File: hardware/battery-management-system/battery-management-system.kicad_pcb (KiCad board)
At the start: 4 copper layers, 100 x 100 mm, 195 parts, among them IC1 LT8584EFE#PBF, IC2 LT8584EFE#PBF, IC3 LT8584EFE#PBF, IC4 LT8584EFE#PBF, J1 VBAT_DISCHARGE, J10 TEMP_CELL4, J2 CELLS, J3 Charge, J4 Discharge, J5 AMPHENOL_micro_usb_10118194-0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, J6 ARM-JTAG-SWD, J7 TEMP_CELL1, J8 TEMP_CELL2, J9 TEMP_CELL3, Q1 TJ40S04M3L, Q10 BS250FTA, Q11 BS250FTA, Q12 BS250FTA, Q13 BS250FTA, Q14 DMN3404L, Q2 TJ40S04M3L, Q3 DMN3404L, Q4 DMN3404L, Q5 DMN3404L, Q6 DMN3404L, Q7 DMN3404L, Q8 BS250FTA, Q9 DMN3404L, T1 NA6252-ALD, T2 NA6252-ALD, T3 NA6252-ALD, T4 NA6252-ALD, U1 STC3100, U10 LM2904M8-13, U11 LM2904M8-13, U2 L6982CDR, U3 L6982CDR, U4 ICL7660, U5 ICL7660, U6 FT230XS, U7 STM32L071CZTx, U8 AT24C512C, U9 NCT75DR2G

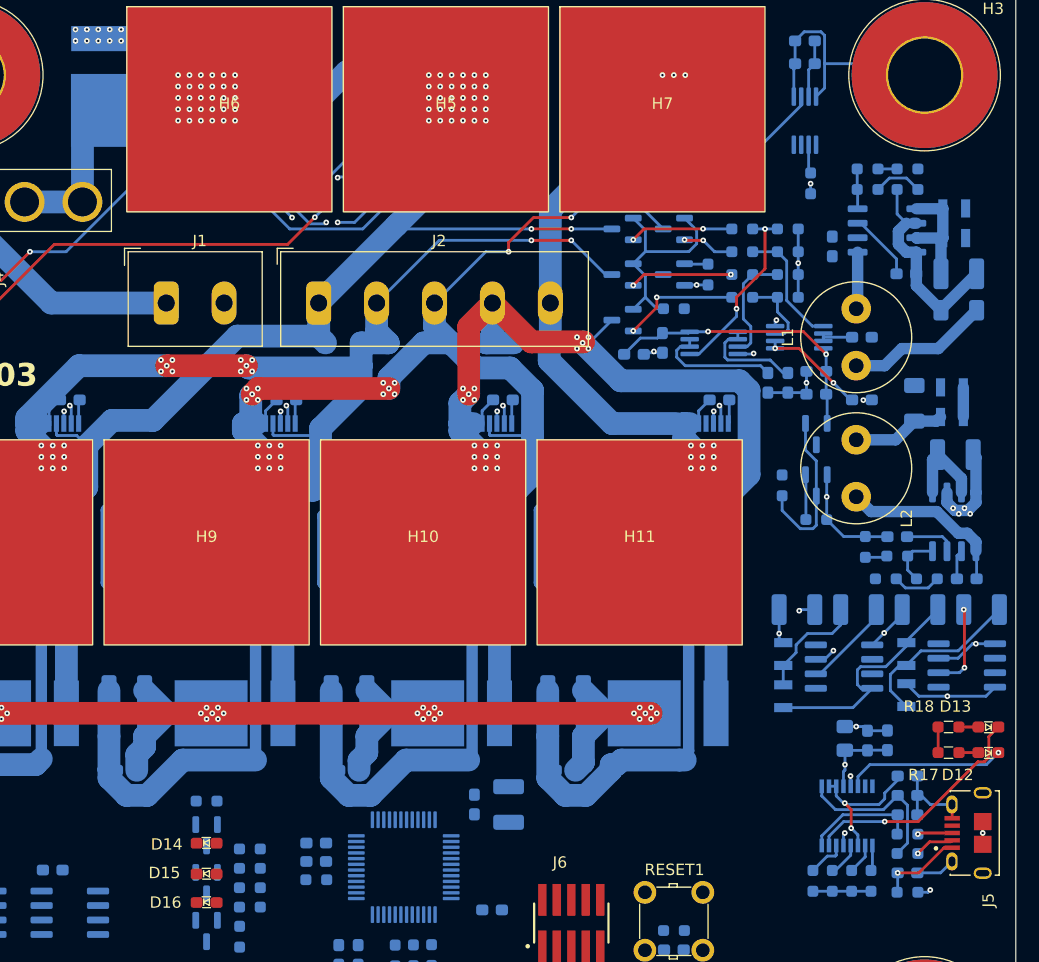
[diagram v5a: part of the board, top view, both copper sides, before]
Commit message: continue work on layout of BMS
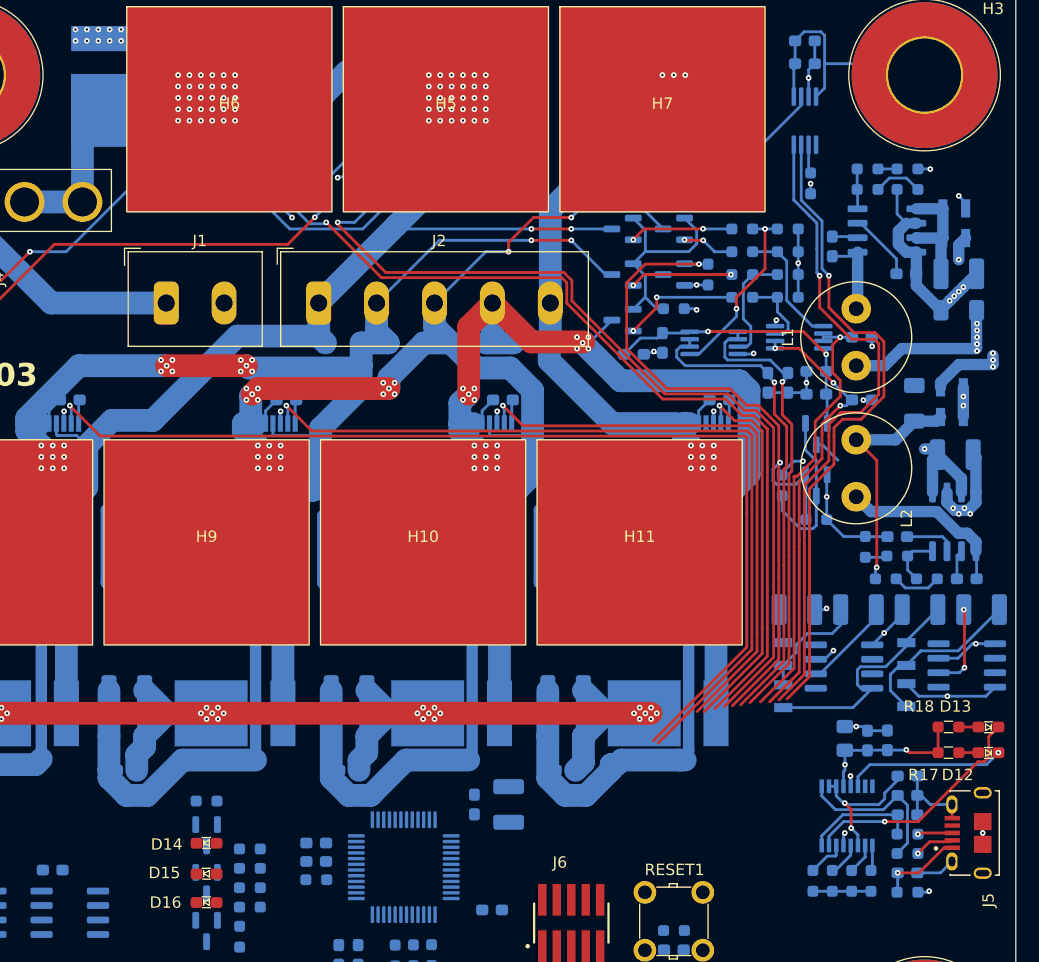
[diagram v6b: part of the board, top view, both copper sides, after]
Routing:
- net /PACK_EXT: track 34.0 -> 128.1 mm, vias 30 -> 32
- net /Cell Balancing/CELL4_ENABLE: track 1.63 -> 92.2 mm
- net /5V_USB: track 10.4 -> 89.9 mm, vias 2 -> 7
- net /DISCHARGE: track 6.10 -> 79.8 mm
- net /CHARGE: track 6.29 -> 79.4 mm
- net /Cell Balancing/CELL3_ENABLE: track 1.63 -> 74.0 mm
- net /EN_CELL_MEASUREMENT: track 6.03 -> 66.4 mm, vias 0 -> 2
- net /MCU/SCL: track 0.00 -> 57.6 mm, vias 0 -> 1
- net /MCU/SDA: track 0.00 -> 57.2 mm, vias 0 -> 1
- net /Cell Balancing/CELL2_ENABLE: track 1.63 -> 51.5 mm
- net /5V: track 11.2 -> 55.8 mm, vias 1 -> 4
- net /Cell Measurement/CELL2: track 3.18 -> 38.9 mm, vias 0 -> 1
- net /Cell Measurement/CELL4: track 11.1 -> 42.6 mm, vias 0 -> 1
- net /Cell Balancing/CELL1_ENABLE: track 1.63 -> 33.0 mm
- net /Cell Measurement/CELL3: track 9.27 -> 40.3 mm, vias 0 -> 1
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
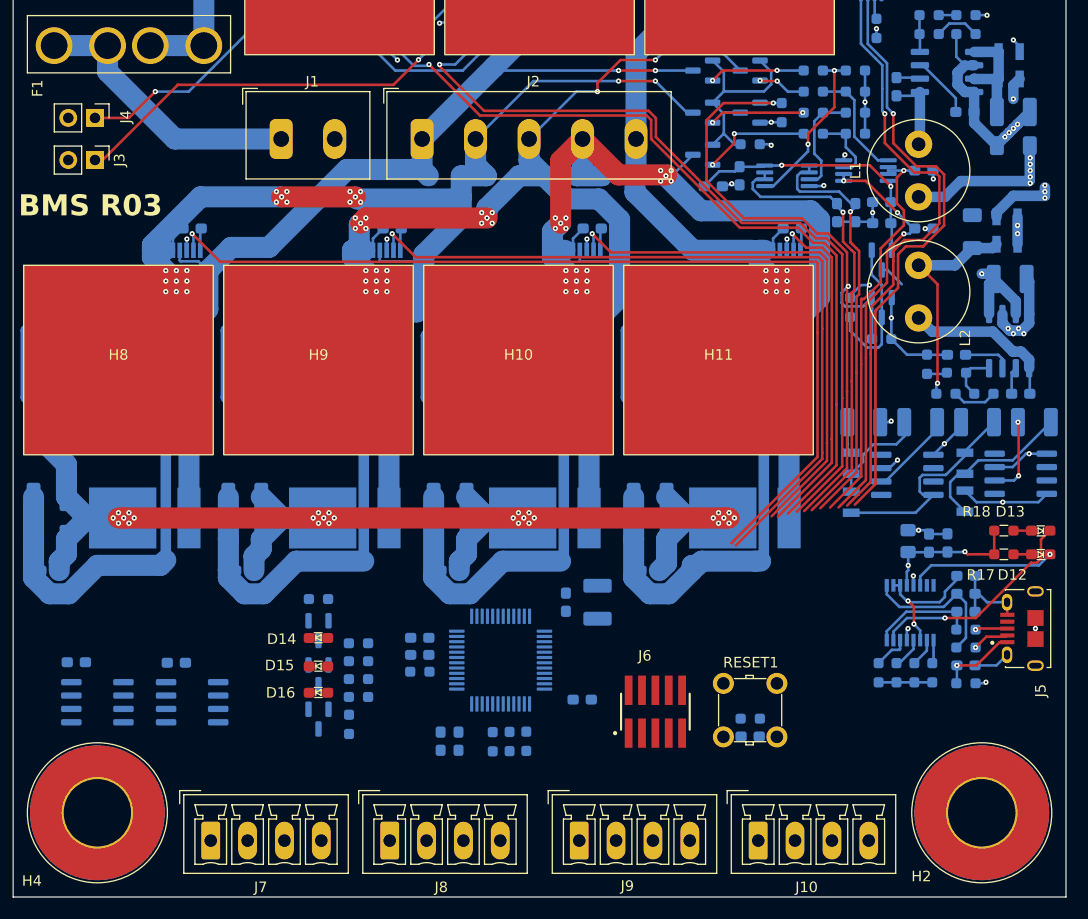
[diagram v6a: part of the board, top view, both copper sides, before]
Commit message: finish layout of BMS
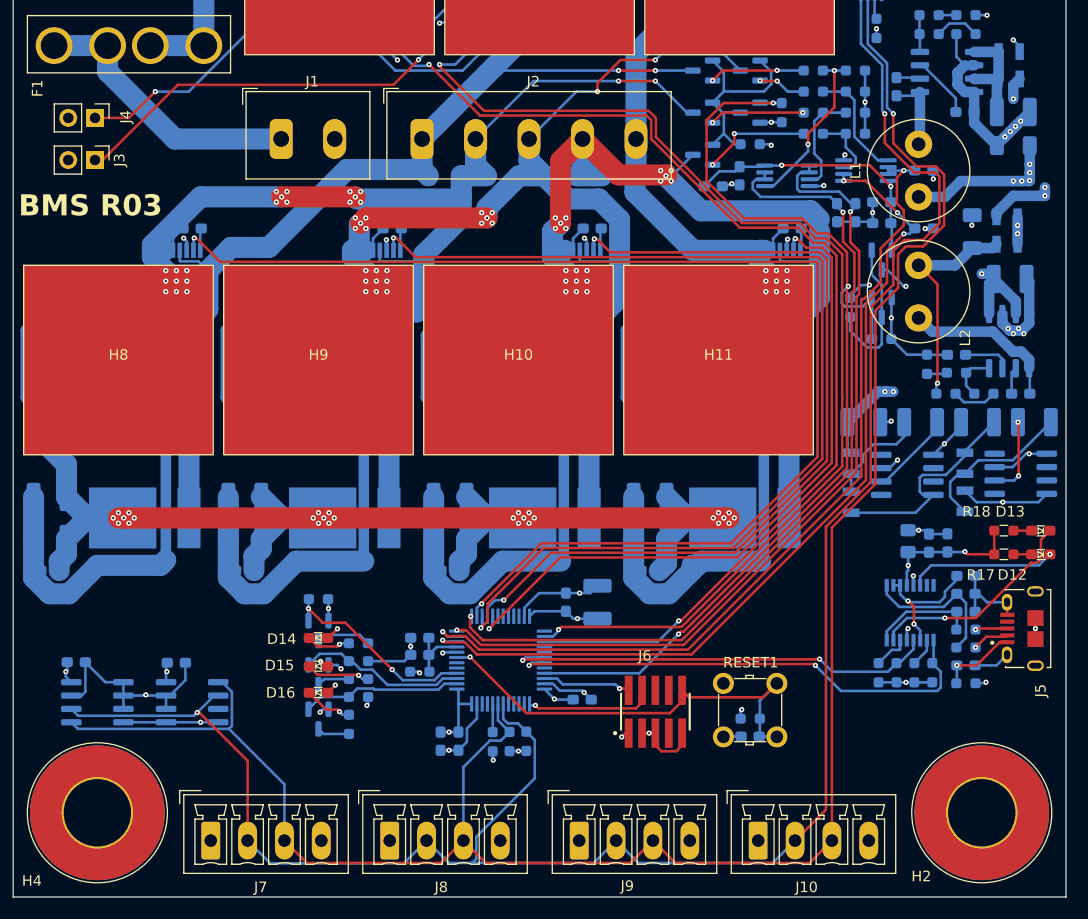
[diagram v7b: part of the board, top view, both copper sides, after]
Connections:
- U7 pad 14: /Cell Balancing/CELL1_ENABLE -> /Cell Balancing/CELL4_ENABLE
- U7 pad 15: /Cell Balancing/CELL2_ENABLE -> /Cell Balancing/CELL3_ENABLE
- U7 pad 16: /Cell Balancing/CELL3_ENABLE -> /Cell Balancing/CELL2_ENABLE
- U7 pad 17: /Cell Balancing/CELL4_ENABLE -> /Cell Balancing/CELL1_ENABLE
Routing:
- net /MCU/SCL: track 57.6 -> 197.8 mm, vias 1 -> 2
- net /MCU/SDA: track 57.2 -> 196.5 mm
- net GND: track 117.1 -> 190.1 mm, vias 45 -> 59
- net /Cell Measurement/CELL1: track 39.1 -> 84.4 mm, vias 3 -> 4
- net /MCU/UART_USB_RX: track 2.24 -> 46.8 mm, vias 0 -> 2
- net /Cell Measurement/CELL2: track 38.9 -> 83.4 mm, vias 1 -> 2
- net /MCU/NRST: track 0.00 -> 42.4 mm, vias 0 -> 1
- net /Cell Measurement/CELL3: track 40.3 -> 80.8 mm, vias 1 -> 2
- net /Cell Measurement/CELL4: track 42.6 -> 81.7 mm, vias 1 -> 2
- net /MCU/UART_USB_TX: track 3.02 -> 41.6 mm, vias 0 -> 2
- net /Cell Balancing/CELL1_ENABLE: track 33.0 -> 65.3 mm, vias 1 -> 2
- net /EN_CELL_MEASUREMENT: track 66.4 -> 97.5 mm, vias 2 -> 3
- net /Cell Balancing/CELL2_ENABLE: track 51.5 -> 82.0 mm, vias 1 -> 2
- net /CHARGE: track 79.4 -> 108.3 mm, vias 1 -> 2
- net /Cell Balancing/CELL3_ENABLE: track 74.0 -> 102.8 mm, vias 1 -> 2
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
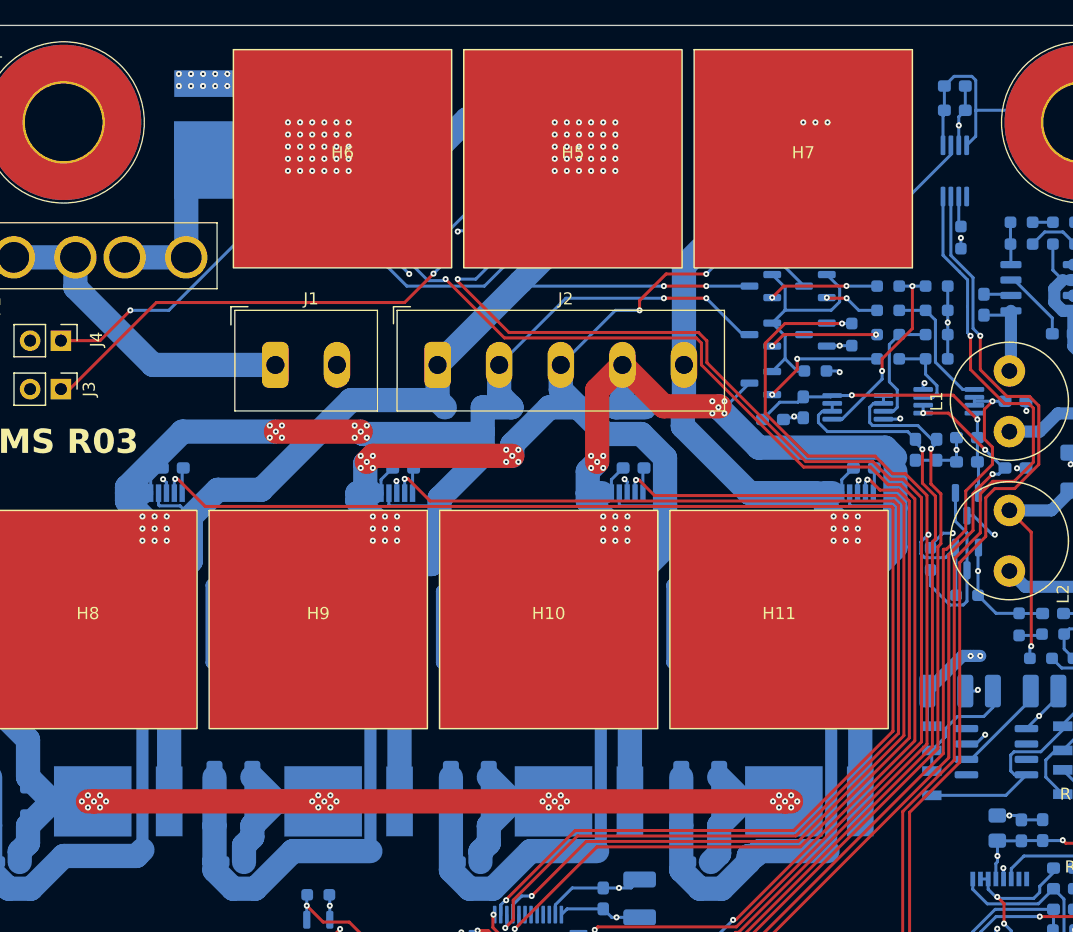
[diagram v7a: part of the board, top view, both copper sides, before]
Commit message: fix silkscreen in BMS layout
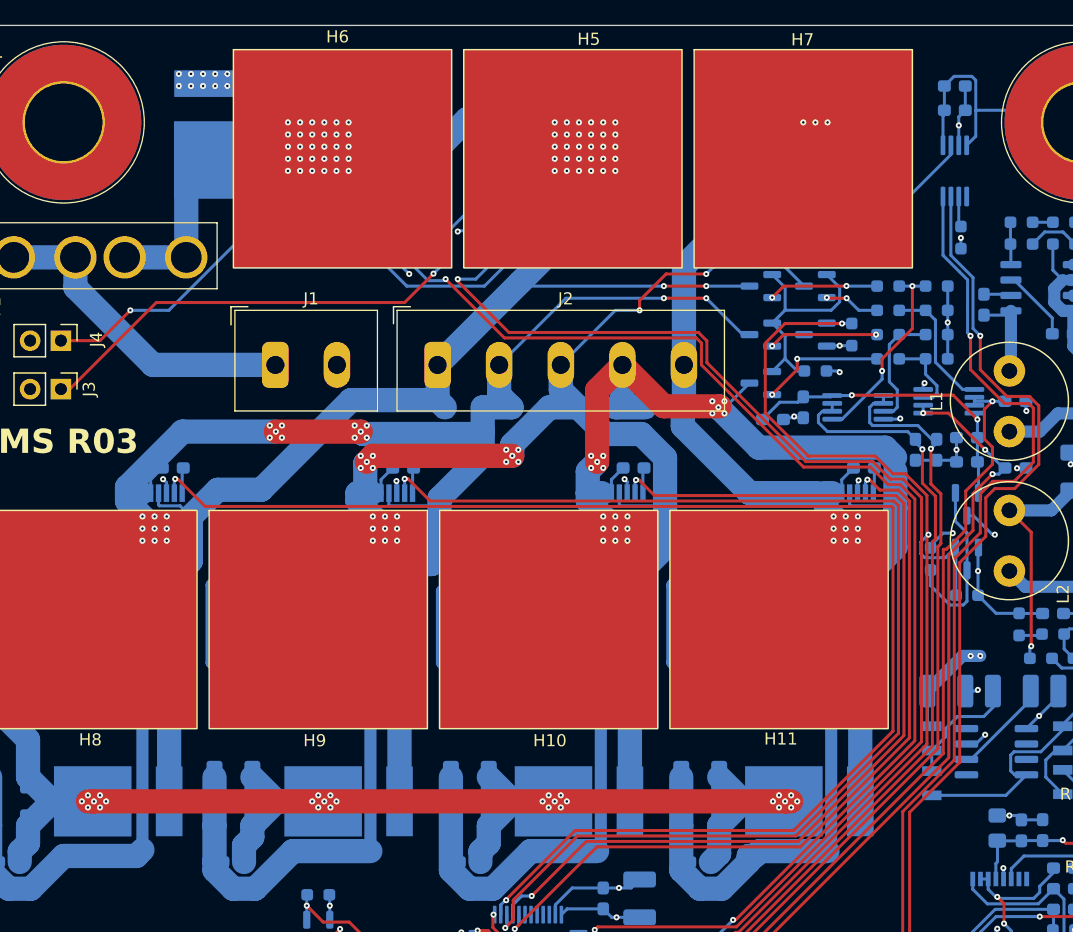
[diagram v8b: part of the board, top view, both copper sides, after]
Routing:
- net /5V_USB: vias 6 -> 5
